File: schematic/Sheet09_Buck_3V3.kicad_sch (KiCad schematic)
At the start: 15 parts, among them U7 ISL70003ASEH

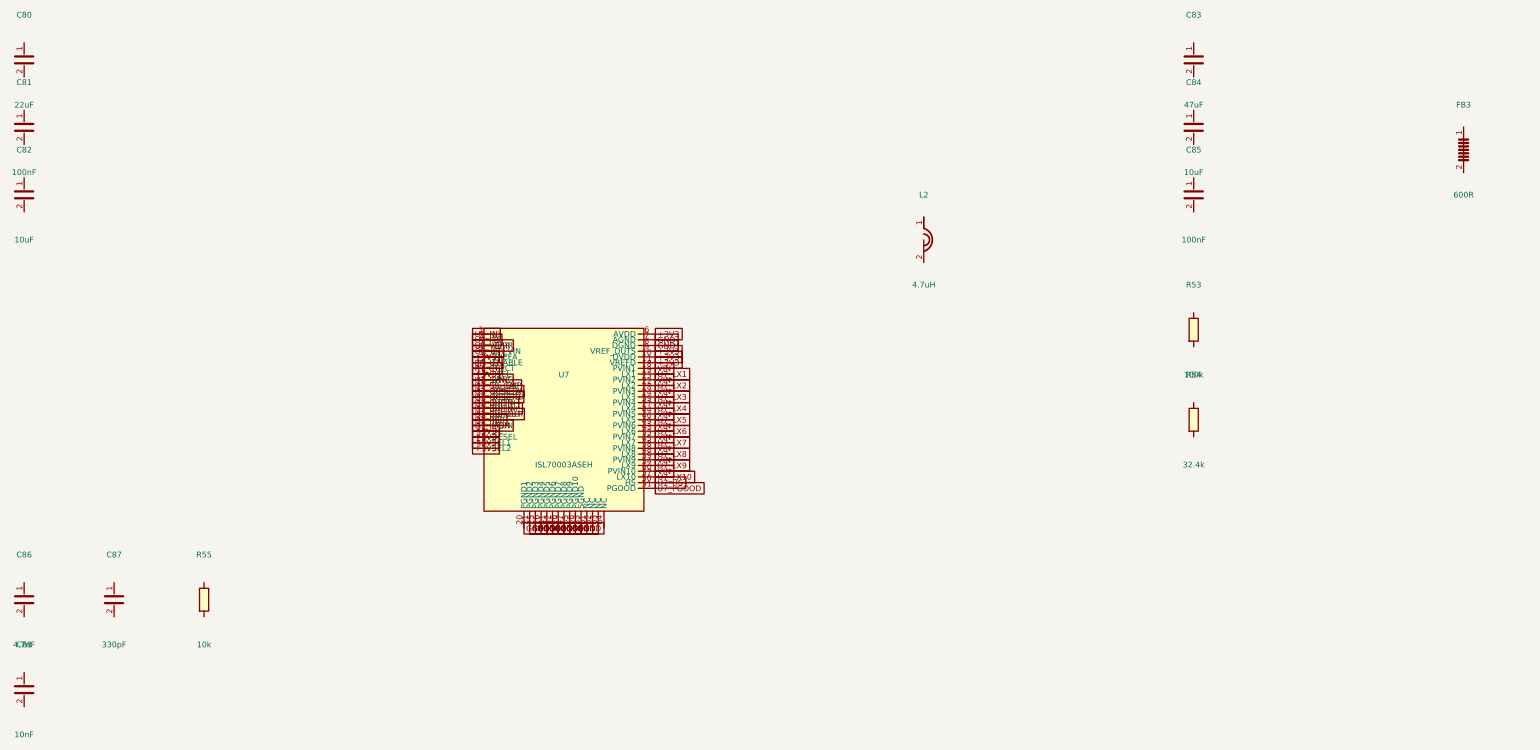
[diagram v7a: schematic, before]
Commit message: feat: connect ALL passive components and fix clock routing
- Added PASSIVE_TOPOLOGY dict mapping 139 passives to their nets
- Passive pin endpoints now get global_labels (was 0 connected, now 138)
- R38 intentionally GND-GND (RECAL_EN pull-down)
- Fixed LMK clock output mapping: CLKout0→ADC_CLK_P, CLKout2→FPGA_REFCLK_P, etc.
- Fixed TPS7H5001-SP SYNC pin collision with LMX_SYNC
- Total connections: 867 pins (up from 641)
- Cross-sheet nets: 52
- Power rails: VIN(33), +3V3(98), GND(228) all with decoupling
- JESD204C: U1↔U2 on 4 lanes ✓
- SPI: U1↔U2↔U3↔U4 ✓
- Clock: LMK→ADC (CLK+SYSREF), LMK→FPGA (REF+SPW) ✓
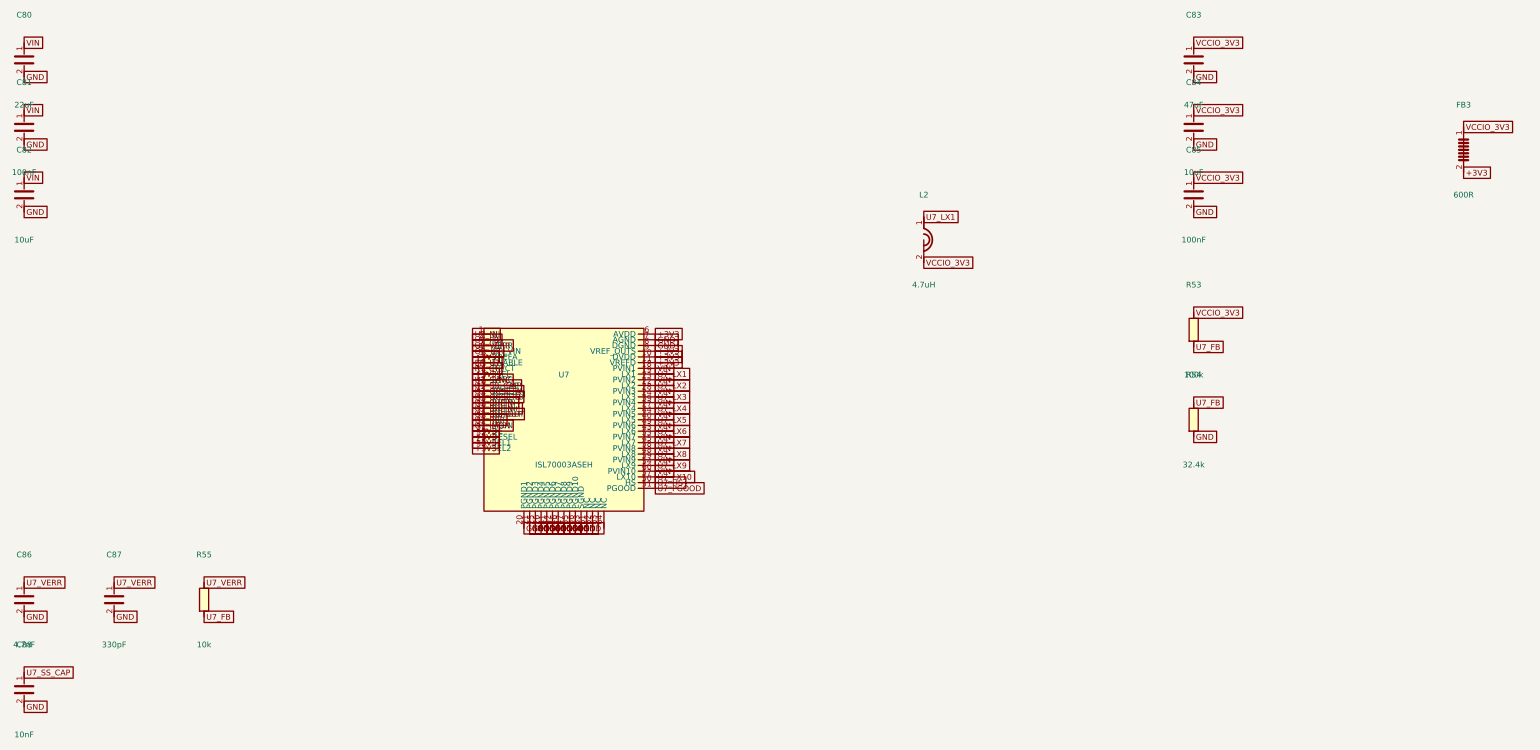
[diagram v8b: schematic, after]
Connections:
- net +3V3: now also FB3.2
- net GND: now also C80.2, C81.2, C82.2, C83.2, C84.2, C85.2, C86.2, C87.2, C88.2, R54.2
- net U7_FB: now also R53.2, R54.1, R55.2
- net U7_LX1: now also L2.1
- net U7_SS_CAP: now also C88.1
- net U7_VERR: now also C86.1, C87.1, R55.1
- net VIN: now also C80.1, C81.1, C82.1
- net VCCIO_3V3: now reaches L2.2
- net VCCIO_3V3: now also C83.1, C84.1, C85.1, FB3.1, R53.1
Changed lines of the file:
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@@
   (global_label "GND" (at 202.5400 144.1300 0) (effects (font (size 1.27 1.27))))
   (global_label "GND" (at 203.8100 144.1300 0) (effects (font (size 1.27 1.27))))
+  (global_label "VIN" (at 80.0000 36.1900 0) (effects (font (size 1.27 1.27))))
+  (global_label "GND" (at 80.0000 43.8100 0) (effects (font (size 1.27 1.27))))
+  (global_label "VIN" (at 80.0000 51.1900 0) (effects (font (size 1.27 1.27))))
+  (global_label "GND" (at 80.0000 58.8100 0) (effects (font (size 1.27 1.27))))
+  (global_label "VIN" (at 80.0000 66.1900 0) (effects (font (size 1.27 1.27))))
+  (global_label "GND" (at 80.0000 73.8100 0) (effects (font (size 1.27 1.27))))
+  (global_label "U7_LX1" (at 280.0000 74.9200 0) (effects (font (size 1.27 1.27))))
+  (global_label "VCCIO_3V3" (at 280.0000 85.0800 0) (effects (font (size 1.27 1.27))))
+  (global_label "VCCIO_3V3" (at 340.0000 36.1900 0) (effects (font (size 1.27 1.27))))
+  (global_label "GND" (at 340.0000 43.8100 0) (effects (font (size 1.27 1.27))))
+  (global_label "VCCIO_3V3" (at 340.0000 51.1900 0) (effects (font (size 1.27 1.27))))
+  (global_label "GND" (at 340.0000 58.8100 0) (effects (font (size 1.27 1.27))))
+  (global_label "VCCIO_3V3" (at 340.0000 66.1900 0) (effects (font (size 1.27 1.27))))
+  (global_label "GND" (at 340.0000 73.8100 0) (effects (font (size 1.27 1.27))))
+  (global_label "VCCIO_3V3" (at 340.0000 96.1900 0) (effects (font (size 1.27 1.27))))
+  (global_label "U7_FB" (at 340.0000 103.8100 0) (effects (font (size 1.27 1.27))))
+  (global_label "U7_FB" (at 340.0000 116.1900 0) (effects (font (size 1.27 1.27))))
+  (global_label "GND" (at 340.0000 123.8100 0) (effects (font (size 1.27 1.27))))
+  (global_label "U7_VERR" (at 80.0000 156.1900 0) (effects (font (size 1.27 1.27))))
+  (global_label "GND" (at 80.0000 163.8100 0) (effects (font (size 1.27 1.27))))
+  (global_label "U7_VERR" (at 100.0000 156.1900 0) (effects (font (size 1.27 1.27))))
+  (global_label "GND" (at 100.0000 163.8100 0) (effects (font (size 1.27 1.27))))
+  (global_label "U7_VERR" (at 120.0000 156.1900 0) (effects (font (size 1.27 1.27))))
+  (global_label "U7_FB" (at 120.0000 163.8100 0) (effects (font (size 1.27 1.27))))
+  (global_label "U7_SS_CAP" (at 80.0000 176.1900 0) (effects (font (size 1.27 1.27))))
+  (global_label "GND" (at 80.0000 183.8100 0) (effects (font (size 1.27 1.27))))
+  (global_label "VCCIO_3V3" (at 400.0000 54.9200 0) (effects (font (size 1.27 1.27))))
+  (global_label "+3V3" (at 400.0000 65.0800 0) (effects (font (size 1.27 1.27))))
   (sheet_instances (path "/" (page "1")))
 )
